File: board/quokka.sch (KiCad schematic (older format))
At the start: 0 parts

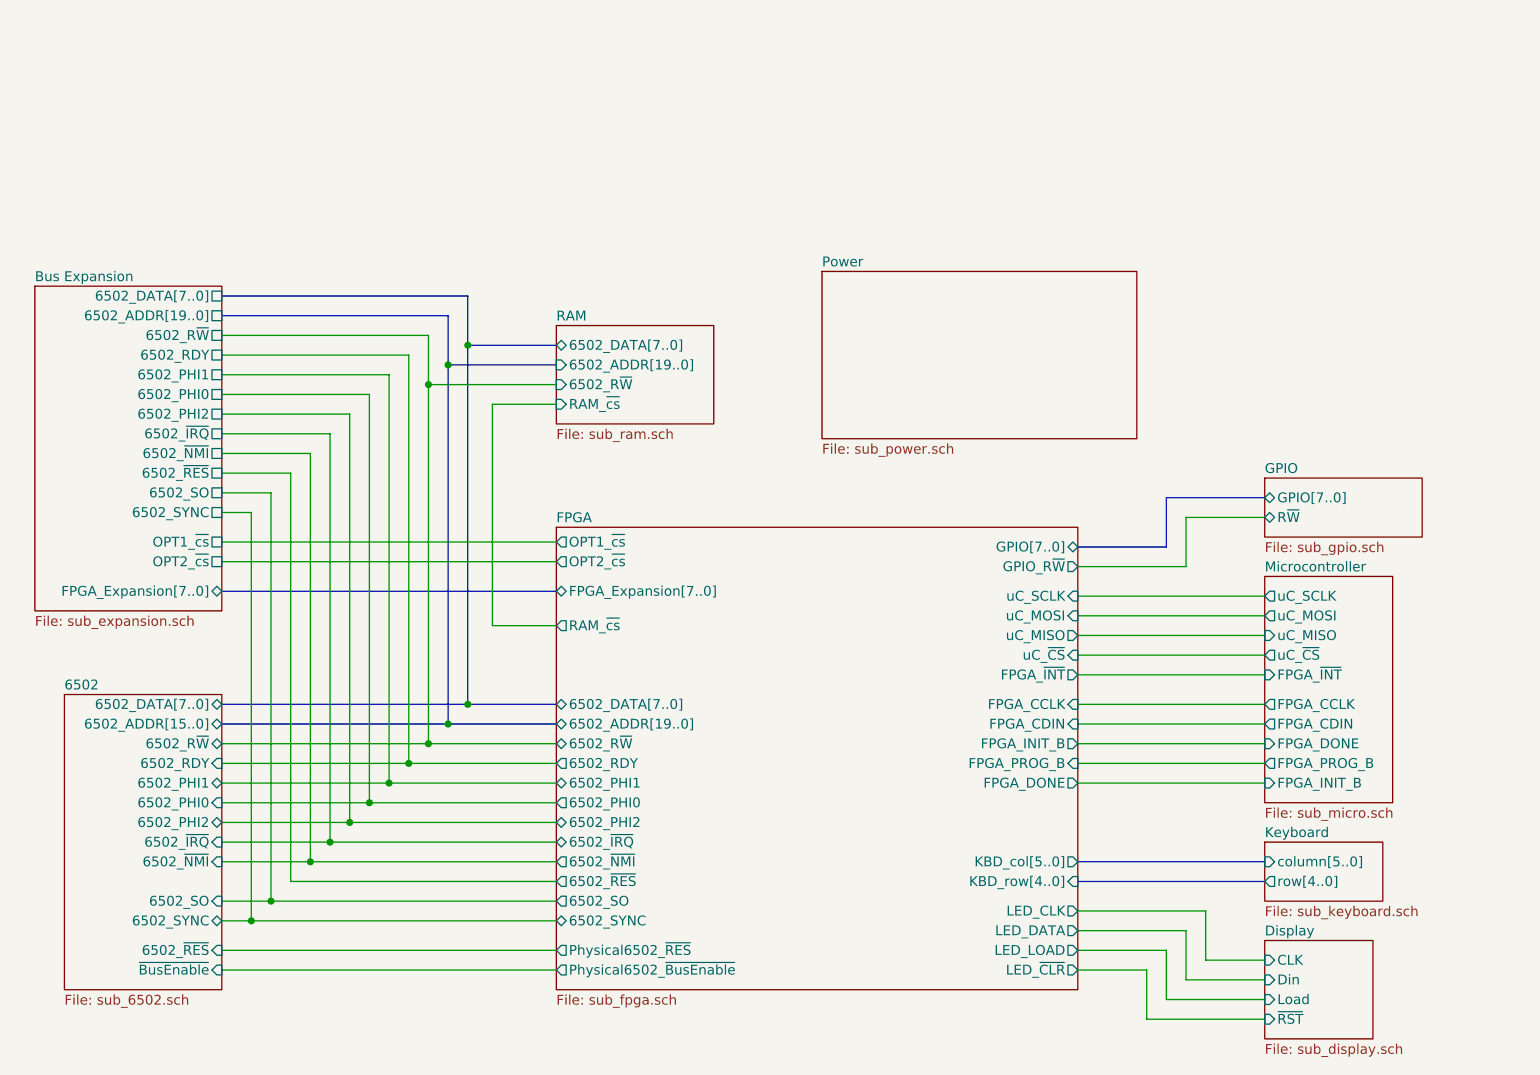
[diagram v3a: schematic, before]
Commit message: Added SPI Flash for uC
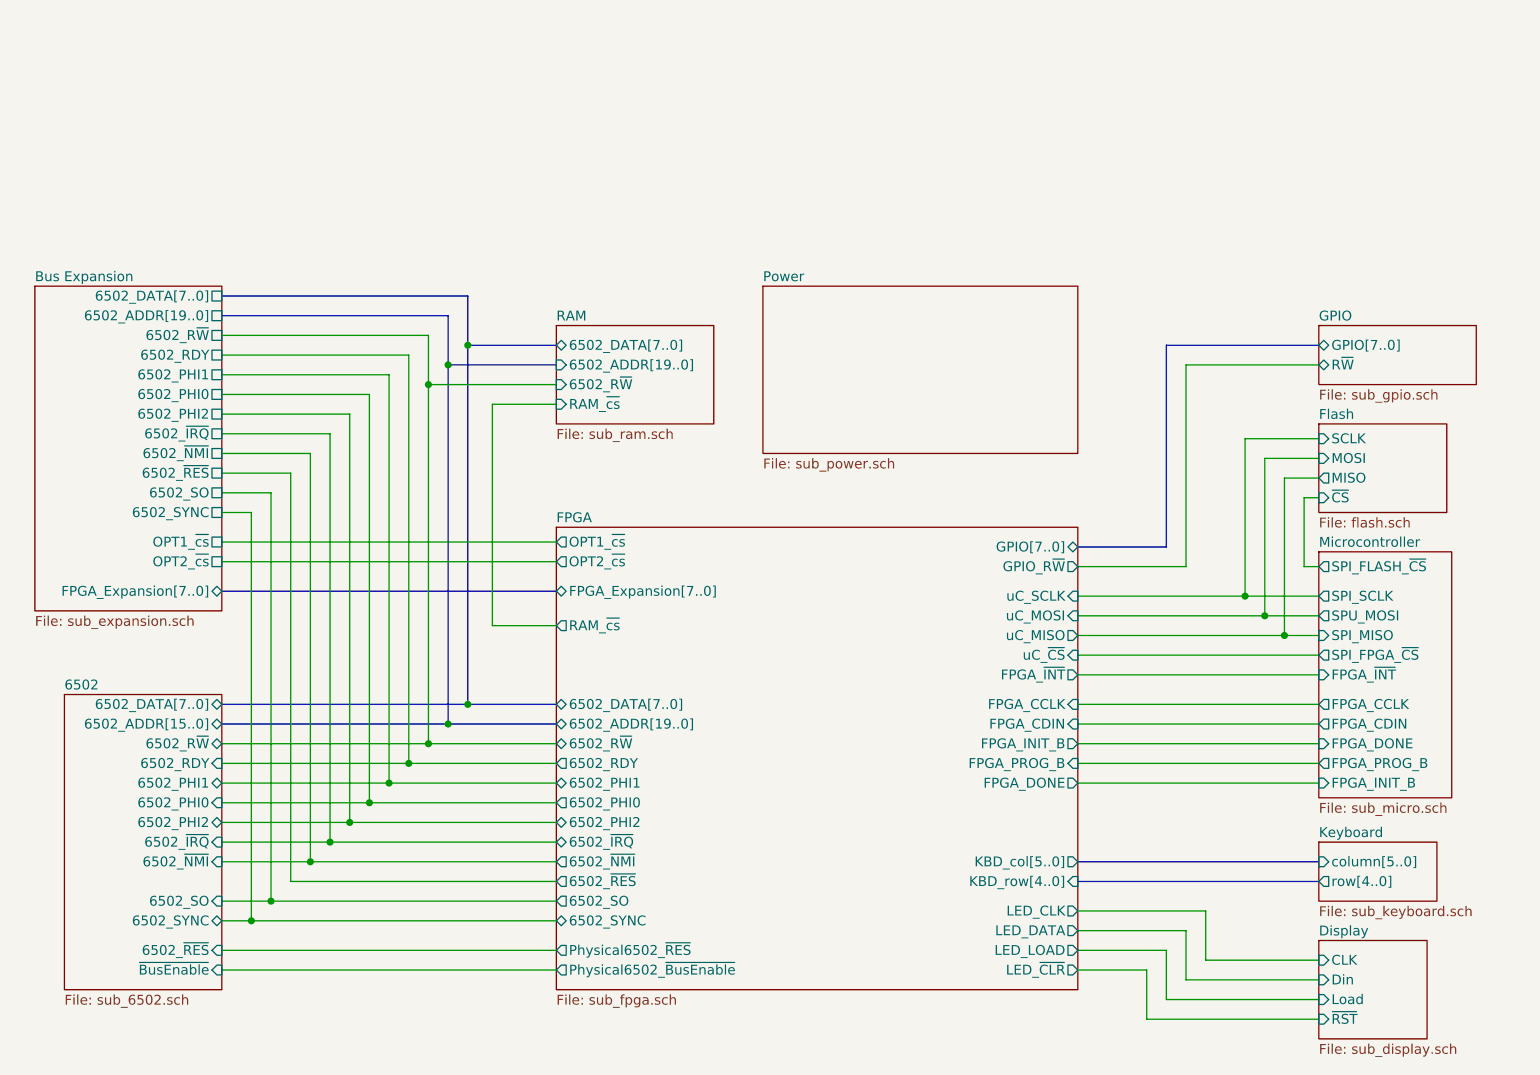
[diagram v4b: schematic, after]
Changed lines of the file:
@@
 $Descr USLetter 11000 8500
 encoding utf-8
-Sheet 1 14
+Sheet 1 15
 Title ""
 Date ""
@@
 $EndDescr
 $Sheet
-S 6100 2675 1600 850
+S 5800 2750 1600 850
 U 5A9C14CE
 F0 "Power" 50
@@
 $EndSheet
 $Sheet
-S 8350 4225 650  1150
+S 8625 4100 675  1250
 U 5A9C14E5
 F0 "Microcontroller" 50
 F1 "sub_micro.sch" 50
-F2 "uC_SCLK" O L 8350 4325 50
-F3 "uC_MOSI" O L 8350 4425 50
-F4 "uC_MISO" I L 8350 4525 50
-F5 "uC_~CS" O L 8350 4625 50
-F6 "FPGA_~INT" I L 8350 4725 50
-F7 "FPGA_CCLK" O L 8350 4875 50
-F8 "FPGA_CDIN" O L 8350 4975 50
-F9 "FPGA_DONE" I L 8350 5075 50
-F10 "FPGA_PROG_B" O L 8350 5175 50
-F11 "FPGA_INIT_B" I L 8350 5275 50
-$EndSheet
-$Sheet
-S 8350 3725 800  300
+F2 "FPGA_~INT" I L 8625 4725 50
+F3 "FPGA_CCLK" O L 8625 4875 50
+F4 "FPGA_CDIN" O L 8625 4975 50
+F5 "FPGA_DONE" I L 8625 5075 50
+F6 "FPGA_PROG_B" O L 8625 5175 50
+F7 "FPGA_INIT_B" I L 8625 5275 50
+F8 "SPI_SCLK" O L 8625 4325 50
+F9 "SPU_MOSI" O L 8625 4425 50
+F10 "SPI_MISO" I L 8625 4525 50
+F11 "SPI_FPGA_~CS" O L 8625 4625 50
+F12 "SPI_FLASH_~CS" O L 8625 4175 50
+$EndSheet
+$Sheet
+S 8625 2950 800  300
 U 5A9C14FD
 F0 "GPIO" 50
 F1 "sub_gpio.sch" 50
-F2 "R~W" B L 8350 3925 50
-F3 "GPIO[7..0]" B L 8350 3825 50
-$EndSheet
-$Sheet
-S 8350 6075 550  500
+F2 "R~W" B L 8625 3150 50
+F3 "GPIO[7..0]" B L 8625 3050 50
+$EndSheet
+$Sheet
+S 8625 6075 550  500
 U 5A9C150A
 F0 "Display" 50
 F1 "sub_display.sch" 50
-F2 "CLK" I L 8350 6175 50
-F3 "~RST" I L 8350 6475 50
-F4 "Load" I L 8350 6375 50
-F5 "Din" I L 8350 6275 50
-$EndSheet
-$Sheet
-S 8350 5575 600  300
+F2 "CLK" I L 8625 6175 50
+F3 "~RST" I L 8625 6475 50
+F4 "Load" I L 8625 6375 50
+F5 "Din" I L 8625 6275 50
+$EndSheet
+$Sheet
+S 8625 5575 600  300
 U 5A9C1519
 F0 "Keyboard" 50
 F1 "sub_keyboard.sch" 50
-F2 "column[5..0]" I L 8350 5675 50
-F3 "row[4..0]" O L 8350 5775 50
+F2 "column[5..0]" I L 8625 5675 50
+F3 "row[4..0]" O L 8625 5775 50
 $EndSheet
 $Sheet
@@
 $EndSheet
 Wire Wire Line
-	8350 4325 7400 4325
+	8625 4325 8250 4325
 Wire Wire Line
 	7400 4425 8350 4425
 Wire Wire Line
-	8350 4525 7400 4525
-Wire Wire Line
-	7400 4625 8350 4625
-Wire Wire Line
-	8350 4725 7400 4725
-Wire Wire Line
-	7400 4875 8350 4875
-Wire Wire Line
-	8350 4975 7400 4975
-Wire Bus Line
-	7400 5675 8350 5675
-Wire Bus Line
-	7400 5775 8350 5775
-Wire Wire Line
-	8350 6175 8050 6175
+	7400 4625 8625 4625
+Wire Wire Line
+	8625 4725 7400 4725
+Wire Wire Line
+	7400 4875 8625 4875
+Wire Wire Line
+	8625 4975 7400 4975
+Wire Bus Line
+	7400 5675 8625 5675
+Wire Bus Line
+	7400 5775 8625 5775
+Wire Wire Line
+	8625 6175 8050 6175
 Wire Wire Line
 	8050 6175 8050 5925
@@
 	7950 6025 7950 6275
 Wire Wire Line
-	7950 6275 8350 6275
-Wire Wire Line
-	8350 6375 7850 6375
+	7950 6275 8625 6275
+Wire Wire Line
+	8625 6375 7850 6375
 Wire Wire Line
 	7850 6375 7850 6125
@@
 	7750 6225 7750 6475
 Wire Wire Line
-	7750 6475 8350 6475
-Wire Wire Line
-	8350 5075 7400 5075
-Wire Wire Line
-	7400 5175 8350 5175
-Wire Wire Line
-	8350 5275 7400 5275
+	7750 6475 8625 6475
+Wire Wire Line
+	8625 5075 7400 5075
+Wire Wire Line
+	7400 5175 8625 5175
+Wire Wire Line
+	8625 5275 7400 5275
 Wire Bus Line
 	4300 2800 4300 3050
@@
 	7400 4075 7850 4075
 Wire Bus Line
-	7850 4075 7850 3825
-Wire Bus Line
-	7850 3825 8350 3825
-Wire Wire Line
-	8350 3925 7950 3925
-Wire Wire Line
-	7950 3925 7950 4175
+	7850 4075 7850 3050
+Wire Bus Line
+	7850 3050 8625 3050
+Wire Wire Line
+	8625 3150 7950 3150
+Wire Wire Line
+	7950 3150 7950 4175
 Wire Wire Line
 	7950 4175 7400 4175
@@
 Wire Wire Line
 	3050 4050 4750 4050
+$Sheet
+S 8625 3450 650  450
+U 5AAED127
+F0 "Flash" 50
+F1 "flash.sch" 50
+F2 "SCLK" I L 8625 3525 50
+F3 "MOSI" I L 8625 3625 50
+F4 "MISO" O L 8625 3725 50
+F5 "~CS" I L 8625 3825 50
+$EndSheet
+Wire Wire Line
+	8625 4175 8550 4175
+Wire Wire Line
+	8550 4175 8550 3825
+Wire Wire Line
+	8550 3825 8625 3825
+Wire Wire Line
+	8450 3725 8450 4525
+Wire Wire Line
+	8350 3625 8350 4425
+Wire Wire Line
+	8625 3525 8250 3525
+Wire Wire Line
+	8250 3525 8250 4325
+Connection ~ 8250 4325
+Wire Wire Line
+	8250 4325 7400 4325
+Connection ~ 8350 4425
+Wire Wire Line
+	8350 4425 8625 4425
+Connection ~ 8450 4525
+Wire Wire Line
+	8450 4525 7400 4525
+Wire Wire Line
+	8450 4525 8625 4525
+Wire Wire Line
+	8450 3725 8625 3725
+Wire Wire Line
+	8350 3625 8625 3625
 $EndSCHEMATC

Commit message: Power supply routed
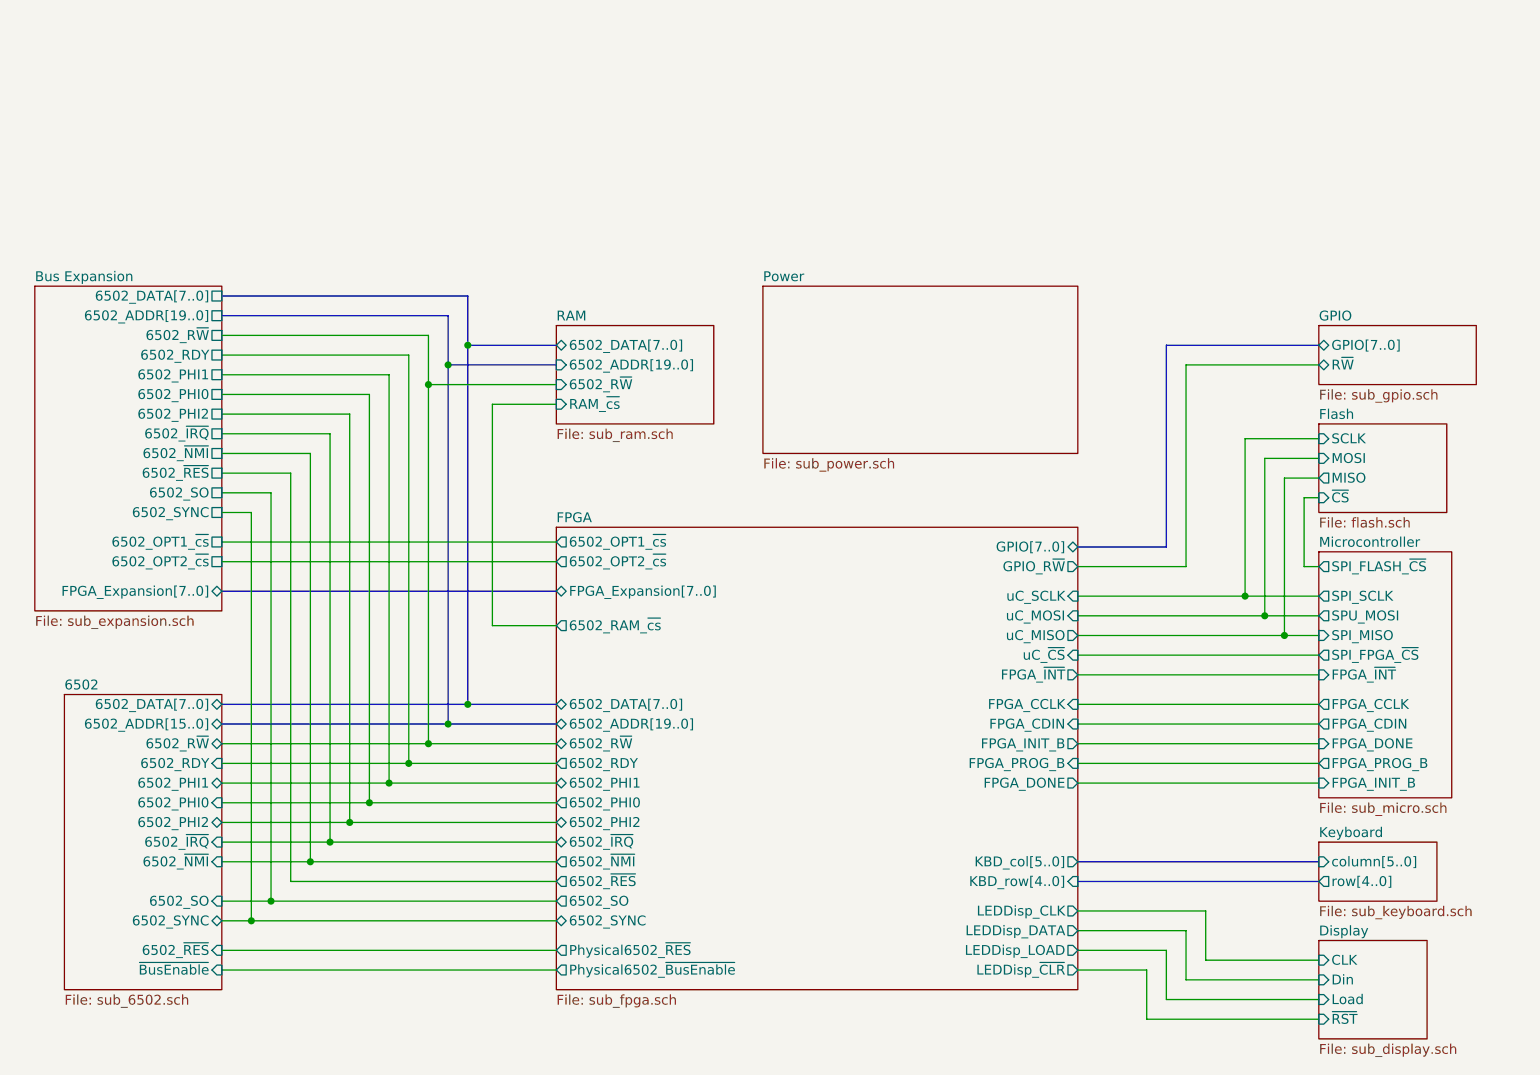
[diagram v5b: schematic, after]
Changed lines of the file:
@@
 F11 "6502_~RES" U R 3050 3700 50
 F12 "6502_SO" U R 3050 3800 50
-F13 "OPT1_~cs" U R 3050 4050 50
-F14 "OPT2_~cs" U R 3050 4150 50
+F13 "6502_OPT1_~cs" U R 3050 4050 50
+F14 "6502_OPT2_~cs" U R 3050 4150 50
 F15 "6502_SYNC" U R 3050 3900 50
 F16 "FPGA_Expansion[7..0]" B R 3050 4300 50
@@
 F4 "6502_DATA[7..0]" T L 4750 4875 50
 F5 "6502_ADDR[19..0]" B L 4750 4975 50
-F6 "RAM_~cs" O L 4750 4475 50
-F7 "OPT1_~cs" O L 4750 4050 50
-F8 "OPT2_~cs" O L 4750 4150 50
+F6 "6502_RAM_~cs" O L 4750 4475 50
+F7 "6502_OPT1_~cs" O L 4750 4050 50
+F8 "6502_OPT2_~cs" O L 4750 4150 50
 F9 "FPGA_Expansion[7..0]" B L 4750 4300 50
-F10 "LED_CLK" O R 7400 5925 50
-F11 "LED_DATA" O R 7400 6025 50
-F12 "LED_LOAD" O R 7400 6125 50
-F13 "6502_R~W" B L 4750 5075 50
-F14 "6502_RDY" O L 4750 5175 50
-F15 "6502_PHI1" B L 4750 5275 50
-F16 "6502_PHI0" O L 4750 5375 50
-F17 "6502_PHI2" B L 4750 5475 50
-F18 "6502_~IRQ" B L 4750 5575 50
-F19 "6502_~NMI" O L 4750 5675 50
-F20 "Physical6502_~RES" O L 4750 6125 50
-F21 "6502_SO" O L 4750 5875 50
-F22 "6502_SYNC" B L 4750 5975 50
-F23 "6502_~RES" O L 4750 5775 50
-F24 "Physical6502_~BusEnable" O L 4750 6225 50
-F25 "uC_SCLK" I R 7400 4325 50
-F26 "uC_MOSI" I R 7400 4425 50
-F27 "uC_MISO" O R 7400 4525 50
-F28 "uC_~CS" I R 7400 4625 50
-F29 "FPGA_~INT" O R 7400 4725 50
-F30 "FPGA_CCLK" I R 7400 4875 50
-F31 "FPGA_CDIN" I R 7400 4975 50
-F32 "LED_~CLR" O R 7400 6225 50
-F33 "FPGA_INIT_B" O R 7400 5075 50
-F34 "FPGA_DONE" O R 7400 5275 50
-F35 "FPGA_PROG_B" I R 7400 5175 50
-F36 "GPIO[7..0]" B R 7400 4075 50
-F37 "GPIO_R~W" O R 7400 4175 50
+F10 "6502_R~W" B L 4750 5075 50
+F11 "6502_RDY" O L 4750 5175 50
+F12 "6502_PHI1" B L 4750 5275 50
+F13 "6502_PHI0" O L 4750 5375 50
+F14 "6502_PHI2" B L 4750 5475 50
+F15 "6502_~IRQ" B L 4750 5575 50
+F16 "6502_~NMI" O L 4750 5675 50
+F17 "Physical6502_~RES" O L 4750 6125 50
+F18 "6502_SO" O L 4750 5875 50
+F19 "6502_SYNC" B L 4750 5975 50
+F20 "6502_~RES" O L 4750 5775 50
+F21 "Physical6502_~BusEnable" O L 4750 6225 50
+F22 "uC_SCLK" I R 7400 4325 50
+F23 "uC_MOSI" I R 7400 4425 50
+F24 "uC_MISO" O R 7400 4525 50
+F25 "uC_~CS" I R 7400 4625 50
+F26 "FPGA_~INT" O R 7400 4725 50
+F27 "FPGA_CCLK" I R 7400 4875 50
+F28 "FPGA_CDIN" I R 7400 4975 50
+F29 "FPGA_INIT_B" O R 7400 5075 50
+F30 "FPGA_DONE" O R 7400 5275 50
+F31 "FPGA_PROG_B" I R 7400 5175 50
+F32 "GPIO[7..0]" B R 7400 4075 50
+F33 "GPIO_R~W" O R 7400 4175 50
+F34 "LEDDisp_CLK" O R 7400 5925 50
+F35 "LEDDisp_DATA" O R 7400 6025 50
+F36 "LEDDisp_LOAD" O R 7400 6125 50
+F37 "LEDDisp_~CLR" O R 7400 6225 50
 $EndSheet
 Wire Wire Line
